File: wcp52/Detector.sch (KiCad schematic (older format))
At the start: 13 parts, among them U11 AD8310ARMZ

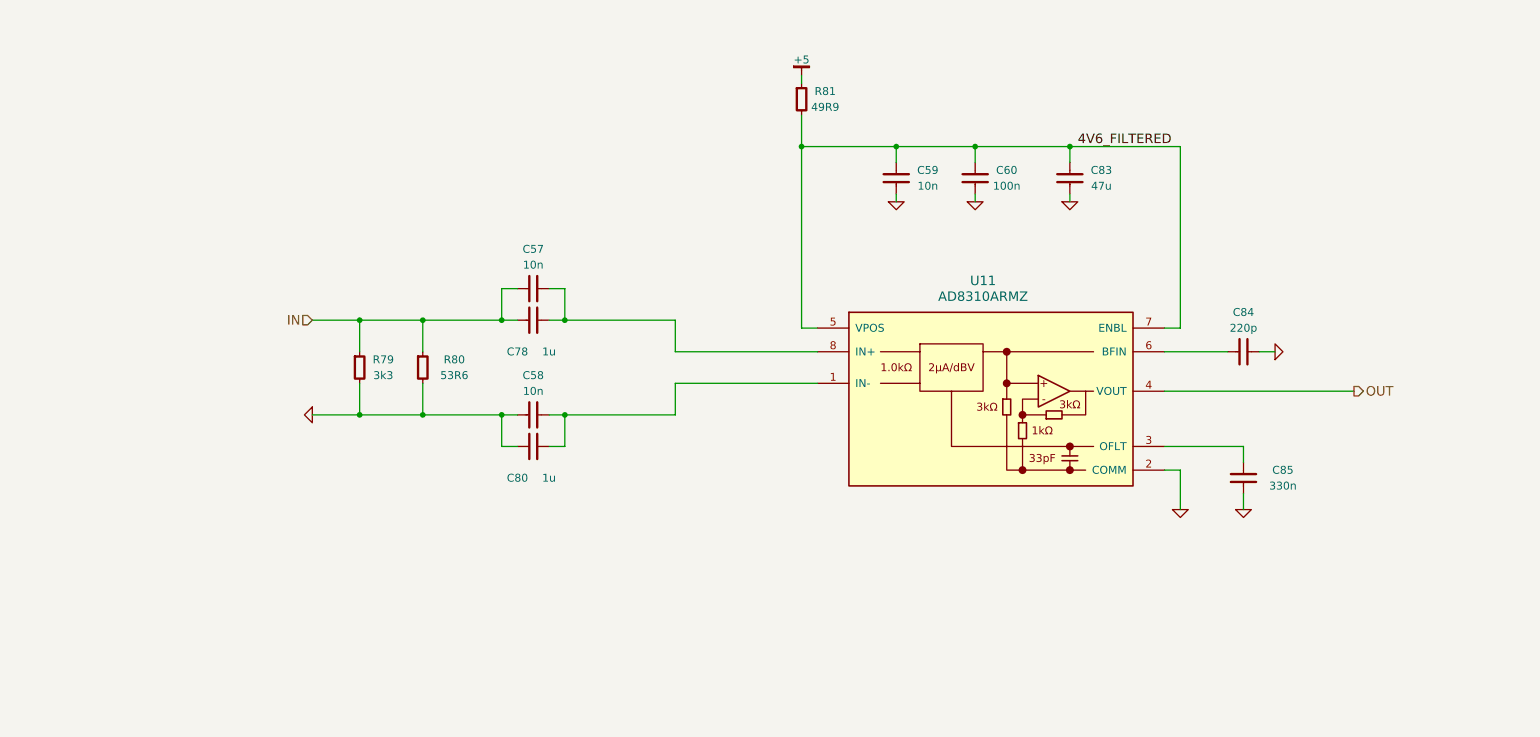
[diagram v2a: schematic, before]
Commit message: Reannotate parts. May need to tweak silkscreen
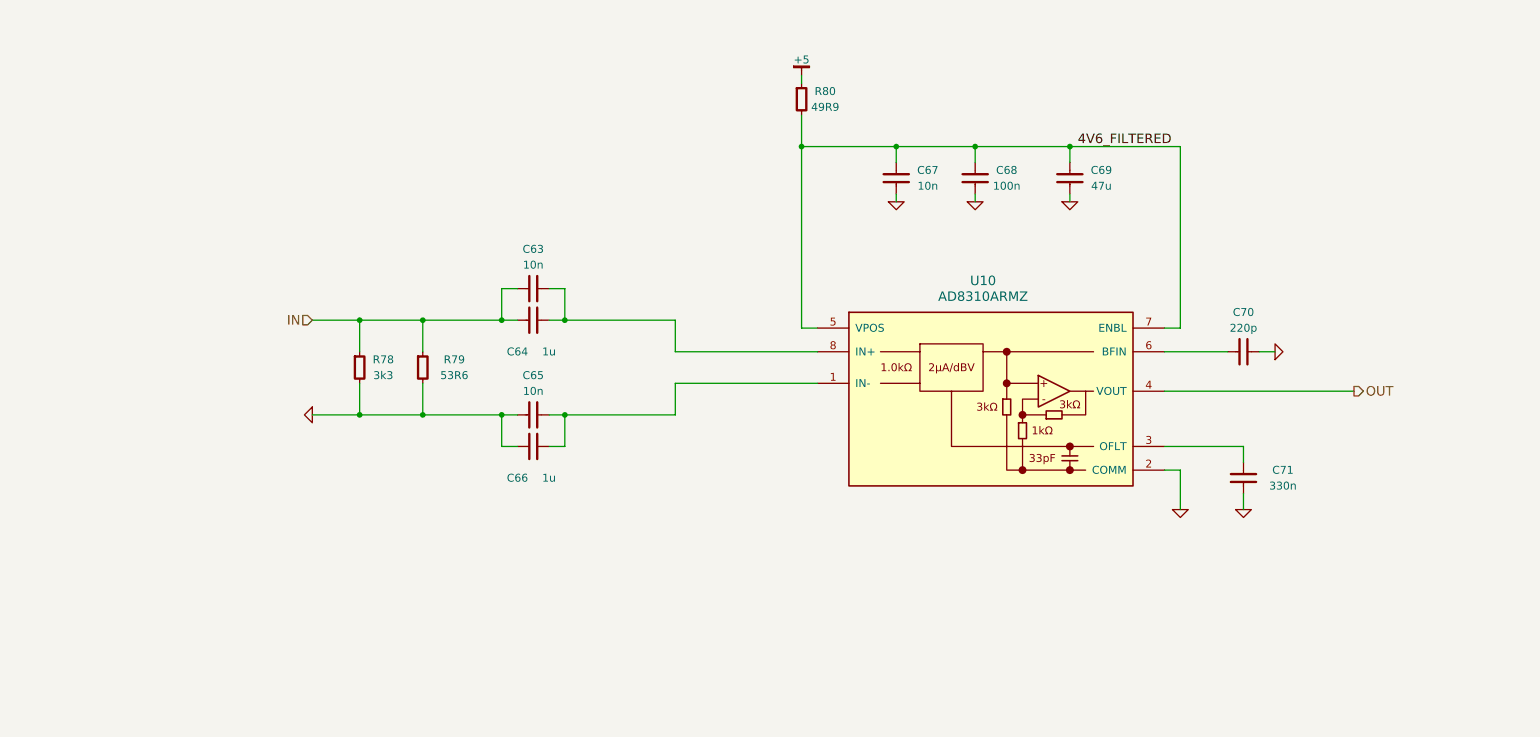
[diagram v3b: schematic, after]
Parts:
- C63: renamed from C57; OldReference (none) -> C57
- C64: renamed from C78; OldReference (none) -> C78
- C65: renamed from C58; OldReference (none) -> C58
- C66: renamed from C80; OldReference (none) -> C80
- C67: renamed from C59; OldReference (none) -> C59
- C68: renamed from C60; OldReference (none) -> C60
- C69: renamed from C83; OldReference (none) -> C83
- C70: renamed from C84; OldReference (none) -> C84
- C71: renamed from C85; OldReference (none) -> C85
- R78: renamed from R79; OldReference (none) -> R79
- R79: renamed from R80; OldReference (none) -> R80
- R80: renamed from R81; OldReference (none) -> R81
- U10: renamed from U11; OldReference (none) -> U11
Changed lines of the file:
@@
 $EndDescr
 $Comp
-L C-0805 C78
+L C-0805 C64
 U 1 1 54F3ADF2
 P 5100 3450
-F 0 "C78" V 5300 3350 50  0000 C CNN
+F 0 "C64" V 5300 3350 50  0000 C CNN
 F 1 "1u" V 5300 3550 50  0000 C CNN
 F 2 "IPC7351-Nominal:CAPC2012X70" H 5100 3450 50  0001 C CNN
@@
 F 5 "TDK" H 5100 3450 60  0001 C CNN "Manuf"
 F 6 "DIST DIGIKEY 445-11490-1-ND" H 5900 4000 60  0001 C CNN "BOM"
+F 7 "C78" H 5100 3450 50  0001 C CNN "OldReference"
 	1    5100 3450
 	0    1    1    0
@@
 Connection ~ 4400 4050
 $Comp
-L C-0805 C80
+L C-0805 C66
 U 1 1 54F3B77F
 P 5100 4250
-F 0 "C80" V 5300 4150 50  0000 C CNN
+F 0 "C66" V 5300 4150 50  0000 C CNN
 F 1 "1u" V 5300 4350 50  0000 C CNN
 F 2 "IPC7351-Nominal:CAPC2012X70" H 5100 4250 50  0001 C CNN
@@
 F 5 "TDK" H 5100 4250 60  0001 C CNN "Manuf"
 F 6 "DIST DIGIKEY 445-11490-1-ND" H 5900 4800 60  0001 C CNN "BOM"
+F 7 "C80" H 5100 4250 50  0001 C CNN "OldReference"
 	1    5100 4250
 	0    1    1    0
@@
 	5200 4050 6000 4050
 $Comp
-L AD8310ARMZ U11
+L AD8310ARMZ U10
 U 1 1 54F22F07
 P 7950 3900
-F 0 "U11" H 7950 4600 60  0000 C CNN
+F 0 "U10" H 7950 4600 60  0000 C CNN
 F 1 "AD8310ARMZ" H 7950 4500 60  0000 C CNN
 F 2 "IPC7351-Nominal:SOP65P490X109-8" H 8050 4050 60  0001 C CNN
@@
 F 5 "AnalogDevices" H 7950 3900 60  0001 C CNN "Manuf"
 F 6 "IC ADI AD8310ARMZ" H 8450 5100 60  0001 C CNN "BOM"
+F 7 "U11" H 7950 3900 50  0001 C CNN "OldReference"
 	1    7950 3900
 	1    0    0    -1
@@
 Connection ~ 5300 4050
 $Comp
-L C-0603 C84
+L C-0603 C70
 U 1 1 54F23275
 P 9600 3650
-F 0 "C84" V 9350 3650 50  0000 C CNN
+F 0 "C70" V 9350 3650 50  0000 C CNN
 F 1 "220p" V 9450 3650 50  0000 C CNN
 F 2 "IPC7351-Nominal:CAPC1608X55" H 9600 3650 50  0001 C CNN
@@
 F 4 "Value" H 9600 3650 60  0001 C CNN "Manuf"
 F 5 "CAP MLCC 220p C0G 16V 5% [0603]" H 10400 4200 60  0001 C CNN "BOM"
+F 6 "C84" H 9600 3650 50  0001 C CNN "OldReference"
 	1    9600 3650
 	0    1    1    0
@@
 F 2 "" H 9800 3650 60  0000 C CNN
 F 3 "" H 9800 3650 60  0000 C CNN
+F 4 "#PWR0198" H 9800 3650 50  0001 C CNN "OldReference"
 	1    9800 3650
 	0    -1   -1   0
@@
 OUT
 $Comp
-L C-0603 C85
+L C-0603 C71
 U 1 1 54F2346E
 P 9600 4450
-F 0 "C85" H 9850 4500 50  0000 C CNN
+F 0 "C71" H 9850 4500 50  0000 C CNN
 F 1 "330n" H 9850 4400 50  0000 C CNN
 F 2 "IPC7351-Nominal:CAPC1608X55" H 9600 4450 50  0001 C CNN
@@
 F 4 "Value" H 9600 4450 60  0001 C CNN "Manuf"
 F 5 "CAP MLCC 330n ≥X7R 50V 5% [0603]" H 10400 5000 60  0001 C CNN "BOM"
+F 6 "C85" H 9600 4450 50  0001 C CNN "OldReference"
 	1    9600 4450
 	1    0    0    -1
@@
 F 2 "" H 9600 4650 60  0000 C CNN
 F 3 "" H 9600 4650 60  0000 C CNN
+F 4 "#PWR0199" H 9600 4650 50  0001 C CNN "OldReference"
 	1    9600 4650
 	1    0    0    -1
@@
 F 2 "" H 9200 4650 60  0000 C CNN
 F 3 "" H 9200 4650 60  0000 C CNN
+F 4 "#PWR0200" H 9200 4650 50  0001 C CNN "OldReference"
 	1    9200 4650
 	1    0    0    -1
@@
 	9200 2350 6800 2350
 $Comp
-L C-1206 C83
+L C-1206 C69
 U 1 1 54F2394C
 P 8500 2550
-F 0 "C83" H 8700 2600 50  0000 C CNN
+F 0 "C69" H 8700 2600 50  0000 C CNN
 F 1 "47u" H 8700 2500 50  0000 C CNN
 F 2 "IPC7351-Nominal:CAPC3216X70" H 8500 2550 50  0001 C CNN
@@
 F 4 "Value" H 8500 2550 60  0001 C CNN "Manuf"
 F 5 "CAP MLCC 47u ≥X5R 10V 20% [1206]" H 9300 3100 60  0001 C CNN "BOM"
+F 6 "C83" H 8500 2550 50  0001 C CNN "OldReference"
 	1    8500 2550
 	1    0    0    -1
@@
 F 2 "" H 8500 2700 60  0000 C CNN
 F 3 "" H 8500 2700 60  0000 C CNN
+F 4 "#PWR0201" H 8500 2700 50  0001 C CNN "OldReference"
 	1    8500 2700
 	1    0    0    -1
@@
 F 2 "" H 7900 2700 60  0000 C CNN
 F 3 "" H 7900 2700 60  0000 C CNN
+F 4 "#PWR0202" H 7900 2700 50  0001 C CNN "OldReference"
 	1    7900 2700
 	1    0    0    -1
@@
 F 2 "" H 7400 2700 60  0000 C CNN
 F 3 "" H 7400 2700 60  0000 C CNN
+F 4 "#PWR0203" H 7400 2700 50  0001 C CNN "OldReference"
 	1    7400 2700
 	1    0    0    -1
@@
 F 2 "" H 6800 1900 60  0000 C CNN
 F 3 "" H 6800 1900 60  0000 C CNN
+F 4 "#PWR0204" H 6800 1900 50  0001 C CNN "OldReference"
 	1    6800 1900
 	1    0    0    -1
@@
 F 2 "" H 3700 4050 60  0000 C CNN
 F 3 "" H 3700 4050 60  0000 C CNN
+F 4 "#PWR0205" H 3700 4050 50  0001 C CNN "OldReference"
 	1    3700 4050
 	0    1    1    0
@@
 Connection ~ 4000 4050
 $Comp
-L C-0603 C57
+L C-0603 C63
 U 1 1 54FF63E3
 P 5100 3250
-F 0 "C57" V 5350 3250 50  0000 C CNN
+F 0 "C63" V 5350 3250 50  0000 C CNN
 F 1 "10n" V 5250 3250 50  0000 C CNN
 F 2 "IPC7351-Nominal:CAPC1608X55" H 5100 3250 50  0001 C CNN
@@
 F 4 "Value" H 5100 3250 60  0001 C CNN "Manuf"
 F 5 "CAP MLCC 10n ≥X5R 50V 10% [0603]" H 5900 3800 60  0001 C CNN "BOM"
+F 6 "C57" H 5100 3250 50  0001 C CNN "OldReference"
 	1    5100 3250
 	0    1    -1   0
 $EndComp
 $Comp
-L C-0603 C58
+L C-0603 C65
 U 1 1 54FF6499
 P 5100 4050
-F 0 "C58" V 5350 4050 50  0000 C CNN
+F 0 "C65" V 5350 4050 50  0000 C CNN
 F 1 "10n" V 5250 4050 50  0000 C CNN
 F 2 "IPC7351-Nominal:CAPC1608X55" H 5100 4050 50  0001 C CNN
@@
 F 4 "Value" H 5100 4050 60  0001 C CNN "Manuf"
 F 5 "CAP MLCC 10n ≥X5R 50V 10% [0603]" H 5900 4600 60  0001 C CNN "BOM"
+F 6 "C58" H 5100 4050 50  0001 C CNN "OldReference"
 	1    5100 4050
 	0    1    -1   0
 $EndComp
 $Comp
-L C-0603 C59
+L C-0603 C67
 U 1 1 54FF9496
 P 7400 2550
-F 0 "C59" H 7600 2600 50  0000 C CNN
+F 0 "C67" H 7600 2600 50  0000 C CNN
 F 1 "10n" H 7600 2500 50  0000 C CNN
 F 2 "IPC7351-Nominal:CAPC1608X55" H 7400 2550 50  0001 C CNN
@@
 F 4 "Value" H 7400 2550 60  0001 C CNN "Manuf"
 F 5 "CAP MLCC 10n ≥X5R 50V 10% [0603]" H 8200 3100 60  0001 C CNN "BOM"
+F 6 "C59" H 7400 2550 50  0001 C CNN "OldReference"
 	1    7400 2550
 	1    0    0    -1
 $EndComp
 $Comp
-L C-0603 C60
+L C-0603 C68
 U 1 1 54FFA4C7
 P 7900 2550
-F 0 "C60" H 8100 2600 50  0000 C CNN
+F 0 "C68" H 8100 2600 50  0000 C CNN
 F 1 "100n" H 8100 2500 50  0000 C CNN
 F 2 "IPC7351-Nominal:CAPC1608X55" H 7900 2550 50  0001 C CNN
@@
 F 4 "Value" H 7900 2550 60  0001 C CNN "Manuf"
 F 5 "CAP MLCC 100n ≥X7R 16V 10% [0603]" H 8700 3100 60  0001 C CNN "BOM"
+F 6 "C60" H 7900 2550 50  0001 C CNN "OldReference"
 	1    7900 2550
 	1    0    0    -1
 $EndComp
 $Comp
-L R-0603 R79
+L R-0603 R78
 U 1 1 55030E37
 P 4000 3750
-F 0 "R79" H 4150 3800 50  0000 C CNN
+F 0 "R78" H 4150 3800 50  0000 C CNN
 F 1 "3k3" H 4150 3700 50  0000 C CNN
 F 2 "IPC7351-Nominal:RESC1608X50" H 4000 3750 50  0001 C CNN
@@
 F 4 "Value" H 4000 3750 60  0001 C CNN "Manuf"
 F 5 "RES SMD 3.3k 5% [0603]" H 4750 4300 60  0001 C CNN "BOM"
+F 6 "R79" H 4000 3750 50  0001 C CNN "OldReference"
 	1    4000 3750
 	1    0    0    -1
 $EndComp
 $Comp
-L R-0603 R80
+L R-0603 R79
 U 1 1 55030F3F
 P 4400 3750
-F 0 "R80" H 4600 3800 50  0000 C CNN
+F 0 "R79" H 4600 3800 50  0000 C CNN
 F 1 "53R6" H 4600 3700 50  0000 C CNN
 F 2 "IPC7351-Nominal:RESC1608X50" H 4400 3750 50  0001 C CNN
@@
 F 4 "Value" H 4400 3750 60  0001 C CNN "Manuf"
 F 5 "RES SMD 53.6 1% [0603]" H 5150 4300 60  0001 C CNN "BOM"
+F 6 "R80" H 4400 3750 50  0001 C CNN "OldReference"
 	1    4400 3750
 	1    0    0    -1
 $EndComp
 $Comp
-L R-0603 R81
+L R-0603 R80
 U 1 1 55036177
 P 6800 2050
-F 0 "R81" H 6950 2100 50  0000 C CNN
+F 0 "R80" H 6950 2100 50  0000 C CNN
 F 1 "49R9" H 6950 2000 50  0000 C CNN
 F 2 "IPC7351-Nominal:RESC1608X50" H 6800 2050 50  0001 C CNN
@@
 F 4 "Value" H 6800 2050 60  0001 C CNN "Manuf"
 F 5 "RES SMD 49R9 1% [0603]" H 7550 2600 60  0001 C CNN "BOM"
+F 6 "R81" H 6800 2050 50  0001 C CNN "OldReference"
 	1    6800 2050
 	1    0    0    -1

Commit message: Schematic touchups
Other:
- note added: "Inside shield"
- moved on the sheet: C63, C64, C65, C66, C67, C68, C69, C70, C71, R78, R79, R80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

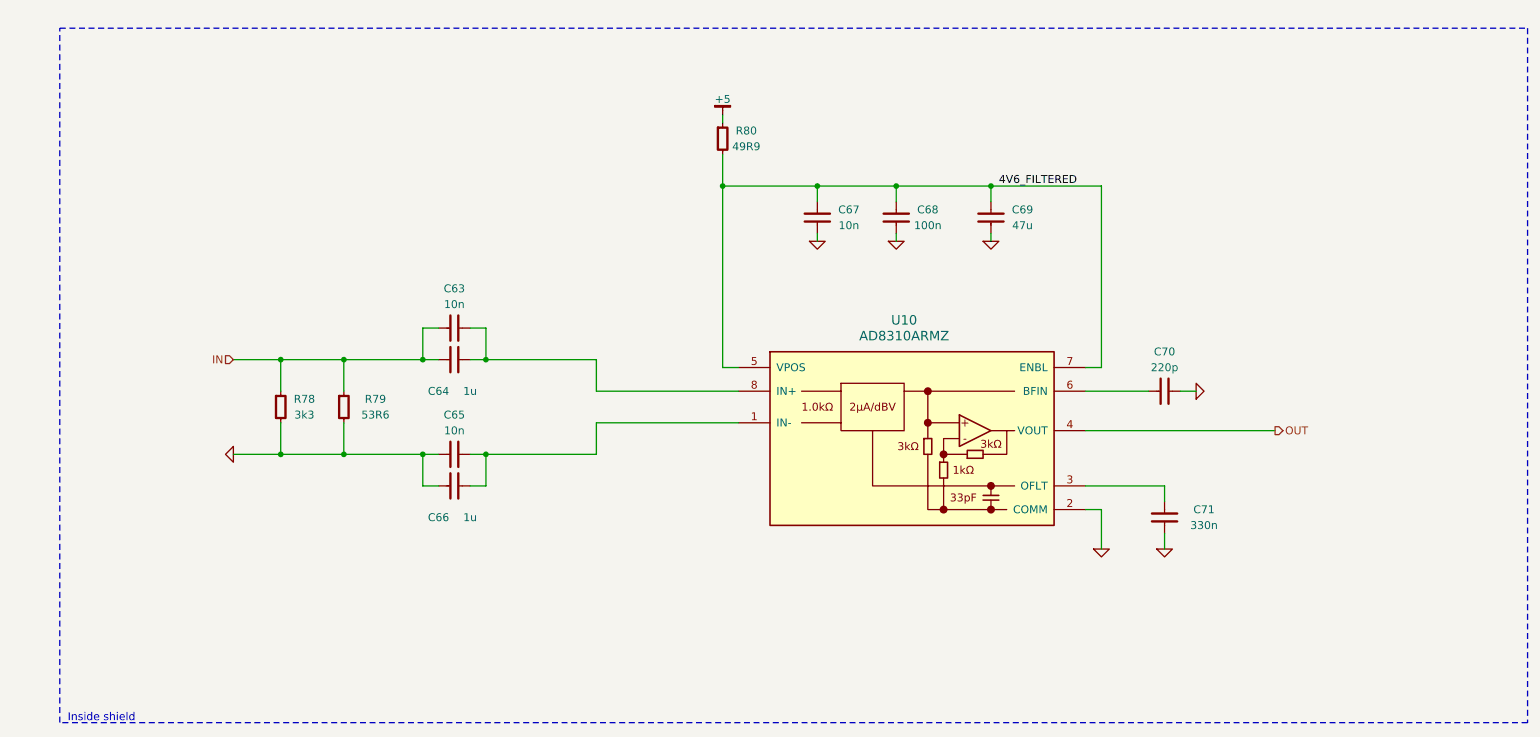
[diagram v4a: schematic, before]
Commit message: Change schematic pages to letter size
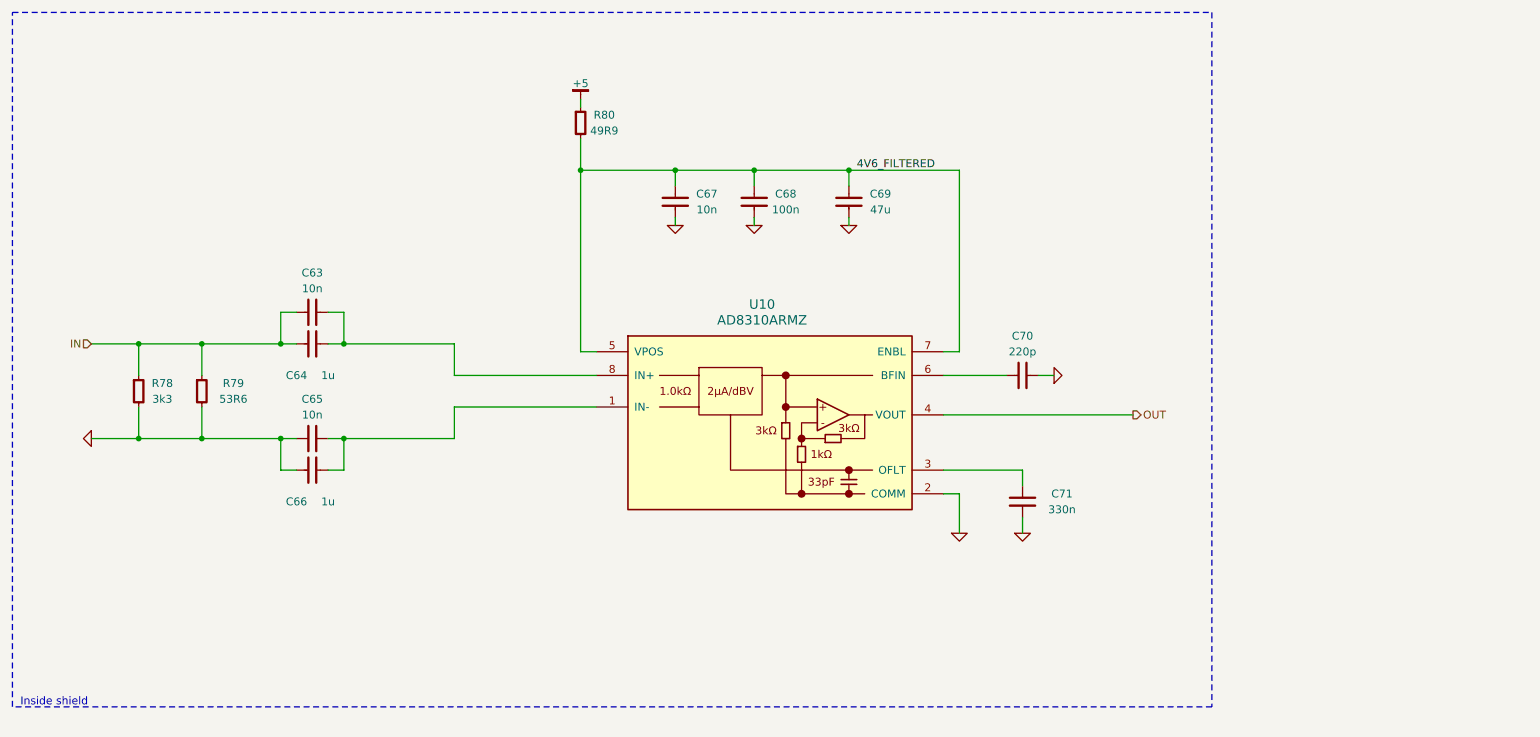
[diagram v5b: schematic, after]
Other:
- moved on the sheet: C63, C64, C65, C66, C67, C68, C69, C70, C71, R78, R79, R80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

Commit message: Correct BOM lines
The BOM reader currently cannot interpret things like '3k3'.
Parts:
- R80: BOM RES SMD 49R9 1% [0603] -> RES SMD 49.9 1% [0603]
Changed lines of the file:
@@
 F 3 "" H 5400 2250 60  0000 C CNN
 F 4 "Value" H 5400 2200 60  0001 C CNN "Manuf"
-F 5 "RES SMD 49R9 1% [0603]" H 6150 2750 60  0001 C CNN "BOM"
+F 5 "RES SMD 49.9 1% [0603]" H 6150 2750 60  0001 C CNN "BOM"
 F 6 "R81" H 5400 2200 50  0001 C CNN "OldReference"
 	1    5400 2200

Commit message: Prepare to fab
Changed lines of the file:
@@
 $EndComp
 Wire Wire Line
-	2300 3600 2600 3600
-Wire Wire Line
-	2600 3600 3000 3600
-Wire Wire Line
-	3000 3600 3500 3600
-Wire Wire Line
-	3500 3600 3600 3600
+	2300 3600 3600 3600
 Wire Wire Line
 	3000 3600 3000 3800
@@
 	2600 4000 2600 4200
 Wire Wire Line
-	2300 4200 2600 4200
-Wire Wire Line
-	2600 4200 3000 4200
-Wire Wire Line
-	3000 4200 3500 4200
-Wire Wire Line
-	3500 4200 3600 4200
+	2300 4200 3600 4200
 Wire Wire Line
 	3000 4000 3000 4200
@@
 	3900 3400 3900 3600
 Wire Wire Line
-	3800 3600 3900 3600
-Wire Wire Line
-	3900 3600 4600 3600
+	3800 3600 4600 3600
 Wire Wire Line
 	3800 4400 3900 4400
@@
 	3900 4400 3900 4200
 Wire Wire Line
-	3800 4200 3900 4200
-Wire Wire Line
-	3900 4200 4600 4200
+	3800 4200 4600 4200
 $Comp
 L AD8310ARMZ U10
@@
 	8100 3800 7700 3800
 $Comp
-L GND #PWR0198
+L GND #PWR0199
 U 1 1 54F233FD
 P 8400 3800
-F 0 "#PWR0198" H 8400 3800 30  0001 C CNN
+F 0 "#PWR0199" H 8400 3800 30  0001 C CNN
 F 1 "GND" H 8400 3730 30  0001 C CNN
 F 2 "" H 8400 3800 60  0000 C CNN
@@
 	8200 4400 7700 4400
 $Comp
-L GND #PWR0199
+L GND #PWR0200
 U 1 1 54F23584
 P 8200 4800
-F 0 "#PWR0199" H 8200 4800 30  0001 C CNN
+F 0 "#PWR0200" H 8200 4800 30  0001 C CNN
 F 1 "GND" H 8200 4730 30  0001 C CNN
 F 2 "" H 8200 4800 60  0000 C CNN
@@
 	8200 4800 8200 4700
 $Comp
-L GND #PWR0200
+L GND #PWR0201
 U 1 1 54F235D2
 P 7800 4800
-F 0 "#PWR0200" H 7800 4800 30  0001 C CNN
+F 0 "#PWR0201" H 7800 4800 30  0001 C CNN
 F 1 "GND" H 7800 4730 30  0001 C CNN
 F 2 "" H 7800 4800 60  0000 C CNN
@@
 	7700 3650 7800 3650
 Wire Wire Line
-	7800 3650 7800 2500
-Wire Wire Line
-	7800 2500 7100 2500
-Wire Wire Line
-	7100 2500 6500 2500
-Wire Wire Line
-	6500 2500 6000 2500
-Wire Wire Line
-	6000 2500 5400 2500
+	7800 2500 7800 3650
+Wire Wire Line
+	5400 2500 7800 2500
 $Comp
 L C-1206 C69
@@
 	7100 2500 7100 2600
 $Comp
-L GND #PWR0201
+L GND #PWR0202
 U 1 1 54F23A44
 P 7100 2850
-F 0 "#PWR0201" H 7100 2850 30  0001 C CNN
+F 0 "#PWR0202" H 7100 2850 30  0001 C CNN
 F 1 "GND" H 7100 2780 30  0001 C CNN
 F 2 "" H 7100 2850 60  0000 C CNN
@@
 	7100 2850 7100 2800
 $Comp
-L GND #PWR0202
+L GND #PWR0203
 U 1 1 54F23F3E
 P 6500 2850
-F 0 "#PWR0202" H 6500 2850 30  0001 C CNN
+F 0 "#PWR0203" H 6500 2850 30  0001 C CNN
 F 1 "GND" H 6500 2780 30  0001 C CNN
 F 2 "" H 6500 2850 60  0000 C CNN
@@
 Connection ~ 6500 2500
 $Comp
-L GND #PWR0203
+L GND #PWR0204
 U 1 1 54F24135
 P 6000 2850
-F 0 "#PWR0203" H 6000 2850 30  0001 C CNN
+F 0 "#PWR0204" H 6000 2850 30  0001 C CNN
 F 1 "GND" H 6000 2780 30  0001 C CNN
 F 2 "" H 6000 2850 60  0000 C CNN
@@
 	5400 3650 5500 3650
 Wire Wire Line
-	5400 2300 5400 2500
-Wire Wire Line
-	5400 2500 5400 3650
+	5400 2300 5400 3650
 Connection ~ 6000 2500
 Connection ~ 5400 2500
 $Comp
-L +5 #PWR0204
+L +5 #PWR0205
 U 1 1 54F24371
 P 5400 2050
-F 0 "#PWR0204" H 5400 2100 30  0001 C CNN
+F 0 "#PWR0205" H 5400 2100 30  0001 C CNN
 F 1 "+5" H 5400 2150 50  0000 C CNN
 F 2 "" H 5400 2050 60  0000 C CNN
@@
 Connection ~ 2600 3600
 $Comp
-L GND #PWR0205
+L GND #PWR0206
 U 1 1 54F24ACA
 P 2300 4200
-F 0 "#PWR0205" H 2300 4200 30  0001 C CNN
+F 0 "#PWR0206" H 2300 4200 30  0001 C CNN
 F 1 "GND" H 2300 4130 30  0001 C CNN
 F 2 "" H 2300 4200 60  0000 C CNN
